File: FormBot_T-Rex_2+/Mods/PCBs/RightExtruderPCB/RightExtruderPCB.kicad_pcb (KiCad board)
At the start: 2 copper layers, 33.2 x 43.2 mm, 9 parts, among them J1 DB15_Control, J2 BL-2, J3 BL-3, J4 FAN_CTL, J5 FAN_AO, J6 EO, J7 Stepper, J8 HEAT

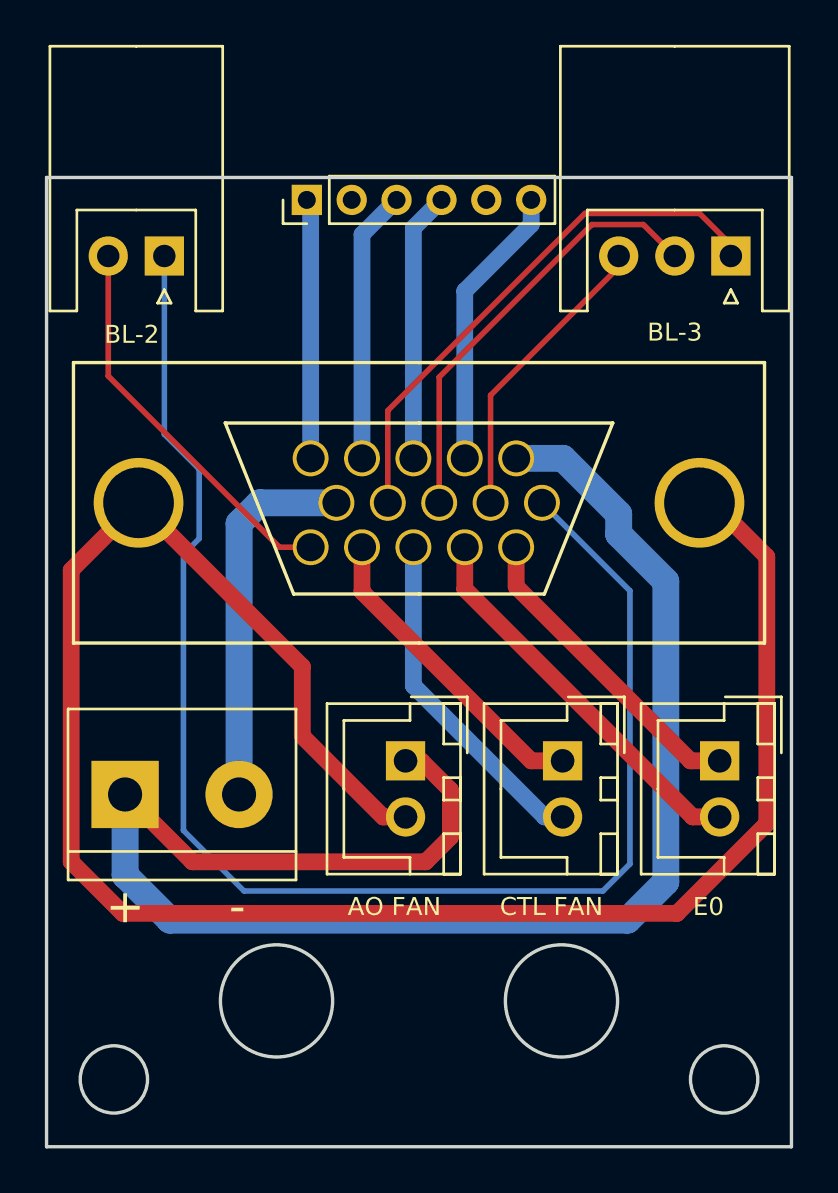
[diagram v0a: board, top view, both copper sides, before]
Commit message: Adding right extruder PCB
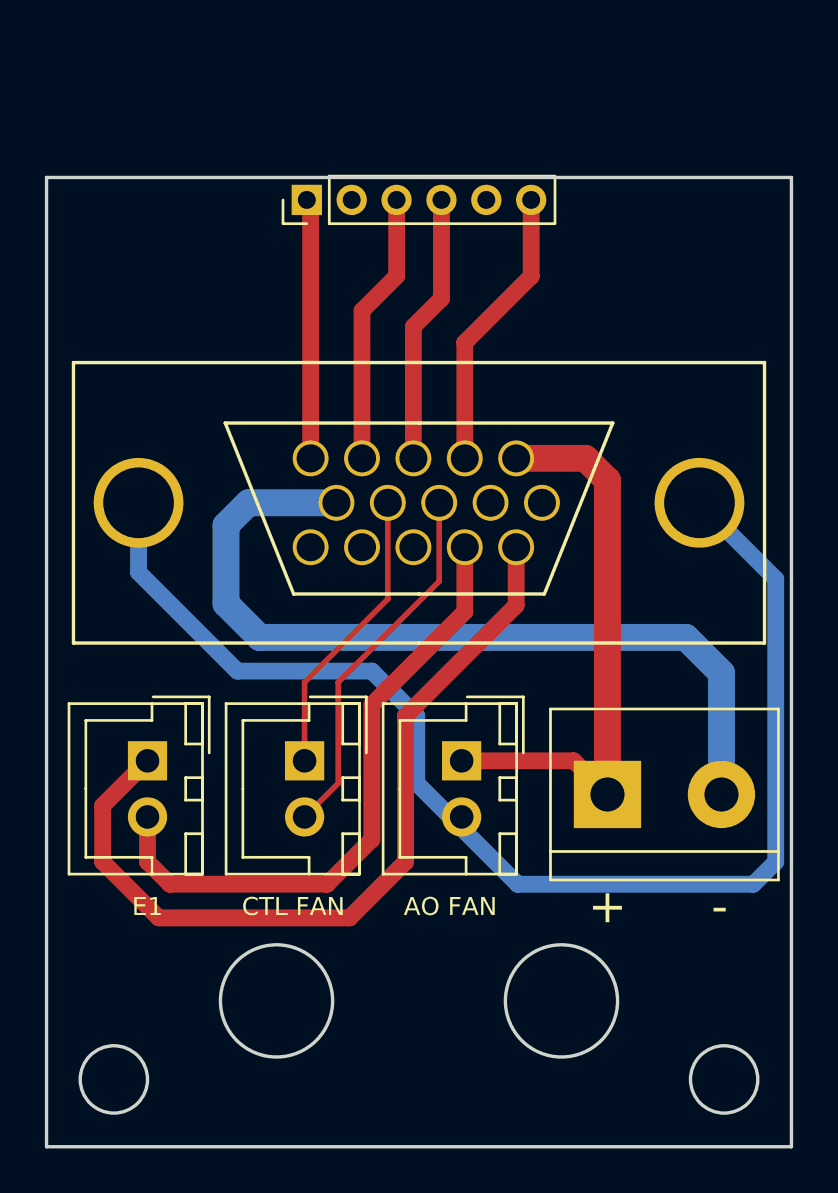
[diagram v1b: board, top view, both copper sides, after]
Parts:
- removed J2: BL-2, Connectors_JST:JST_XH_S02B-XH-A_02x2.50mm_Angled
- removed J3: BL-3, Connectors_JST:JST_XH_S03B-XH-A_03x2.50mm_Angled
- moved J6 25.5 mm to (104.5, 126.0)
- moved J8 21.5 mm to (125.0, 127.5)
- moved J4 11.5 mm to (111.5, 126.0)
- moved J5 2.50 mm to (118.5, 126.0)
- moved G*** 0.90 mm to (108.5, 117.5)
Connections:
- net E0_1 renamed E1_1
- net E0_2 renamed E1_2
- J1 pad 13: FAN_CTL_- -> Net-(J1-Pad13)
- J1 pad 14: FAN_CTL_+ -> Net-(J1-Pad14)
- J1 pad 15: BL2_2 -> Net-(J1-Pad15)
- J1 pad 6: BL2_1 -> Net-(J1-Pad6)
- J1 pad 7: BL3_3 -> Net-(J1-Pad7)
- J1 pad 8: BL3_2 -> FAN_CTL_-
- J1 pad 9: BL3_1 -> FAN_CTL_+
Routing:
- net BL2_1: track 65.8 -> 0.00 mm
- net HEAT_+: track 72.9 -> 25.6 mm
- net GND: track 86.3 -> 57.1 mm
- net BL3_1: track 24.1 -> 0.00 mm
- net E1_1: track 14.0 -> 37.0 mm
- net HEAT_-: track 16.8 -> 37.6 mm
- net BL3_2: track 19.5 -> 0.00 mm
- net BL2_2: track 17.5 -> 0.00 mm
- net BL3_3: track 13.4 -> 0.00 mm
- net E1_2: track 18.1 -> 28.5 mm
- net FAN_CTL_-: track 15.2 -> 16.5 mm
- net FAN_CTL_+: track 14.0 -> 13.0 mm
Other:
- board text added: "E1"
- board text added: "Formbot T-Rex 2+ Extruder PCB - Right"
- board text removed: "BL-2"
- board text removed: "BL-3"
- board text removed: "E0"
- board text removed: "Formbot T-Rex 2+ Extruder PCB - Left"
